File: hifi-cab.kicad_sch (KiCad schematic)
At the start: 0 parts

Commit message: Add RJ45
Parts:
- added J1: RJ45, symbol Connector:RJ45
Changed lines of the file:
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@@
 	(generator_version "9.0")
 	(paper "A4")
+	(symbol
+		(lib_id "Connector:RJ45")
+		(at 92.71 83.82 0)
+		(unit 1)
+		(exclude_from_sim no)
+		(in_bom yes)
+		(on_board yes)
+		(dnp no)
+		(fields_autoplaced yes)
+		(property "Reference" "J1"
+			(at 92.71 66.04 0)
+			(effects
+				(font
+					(size 1.27 1.27)
+				)
+			)
+		)
+		(property "Value" "RJ45"
+			(at 92.71 68.58 0)
+			(effects
+				(font
+					(size 1.27 1.27)
+				)
+			)
+		)
+		(property "Footprint" ""
+			(at 92.71 83.185 90)
+			(effects
+				(font
+					(size 1.27 1.27)
+				)
+				(hide yes)
+			)
+		)
+		(property "Datasheet" "~"
+			(at 92.71 83.185 90)
+			(effects
+				(font
+					(size 1.27 1.27)
+				)
+				(hide yes)
+			)
+		)
+		(property "Description" "RJ connector, 8P8C (8 positions 8 connected)"
+			(at 92.71 83.82 0)
+			(effects
+				(font
+					(size 1.27 1.27)
+				)
+				(hide yes)
+			)
+		)
+		(pin "2"
+		)
+		(pin "3"
+		)
+		(pin "1"
+		)
+		(pin "4"
+		)
+		(pin "5"
+		)
+		(pin "6"
+		)
+		(pin "7"
+		)
+		(pin "8"
+		)
+		(instances
+			(project ""
+				(path "/464ef4ad-8e38-4b55-beb7-b05b4d6675da"
+					(reference "J1")
+					(unit 1)
+				)
+			)
+		)
+	)
 	(sheet_instances
 		(path "/"

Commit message: Update hifi-cab.kicad_sch
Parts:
- removed J1: RJ45, symbol Connector:RJ45
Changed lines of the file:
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@@
 	(generator_version "9.0")
 	(paper "A4")
-	(symbol
-		(lib_id "Connector:RJ45")
-		(at 92.71 83.82 0)
-		(unit 1)
-		(exclude_from_sim no)
-		(in_bom yes)
-		(on_board yes)
-		(dnp no)
-		(fields_autoplaced yes)
-		(property "Reference" "J1"
-			(at 92.71 66.04 0)
-			(effects
-				(font
-					(size 1.27 1.27)
-				)
-			)
-		)
-		(property "Value" "RJ45"
-			(at 92.71 68.58 0)
-			(effects
-				(font
-					(size 1.27 1.27)
-				)
-			)
-		)
-		(property "Footprint" ""
-			(at 92.71 83.185 90)
-			(effects
-				(font
-					(size 1.27 1.27)
-				)
-				(hide yes)
-			)
-		)
-		(property "Datasheet" "~"
-			(at 92.71 83.185 90)
-			(effects
-				(font
-					(size 1.27 1.27)
-				)
-				(hide yes)
-			)
-		)
-		(property "Description" "RJ connector, 8P8C (8 positions 8 connected)"
-			(at 92.71 83.82 0)
-			(effects
-				(font
-					(size 1.27 1.27)
-				)
-				(hide yes)
-			)
-		)
-		(pin "2"
-		)
-		(pin "3"
-		)
-		(pin "1"
-		)
-		(pin "4"
-		)
-		(pin "5"
-		)
-		(pin "6"
-		)
-		(pin "7"
-		)
-		(pin "8"
-		)
-		(instances
-			(project ""
-				(path "/464ef4ad-8e38-4b55-beb7-b05b4d6675da"
-					(reference "J1")
-					(unit 1)
-				)
-			)
-		)
-	)
 	(sheet_instances
 		(path "/"

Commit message: V1 schematic
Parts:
- added D1, D2, D3, D4: 1N4004, Diode_THT:D_DO-41_SOD81_P10.16mm_Horizontal, symbol Diode:1N4004
- added J1: FAN 1, symbol Connector:USB_A
- added J10: BUTTON, symbol Connector:Conn_01x02_Pin
- added J11: RS-232, symbol Connector:Conn_01x04_Pin
- added J12: POWER IN, symbol Connector:Screw_Terminal_01x03
- added J2, J5: FAN VOLTAGE, symbol Connector:Conn_01x03_Pin
- added J3: FAN 1, symbol Connector:Screw_Terminal_01x04
- added J4: FAN 2, symbol Connector:USB_A
- added J6: FAN 2, symbol Connector:Screw_Terminal_01x04
- added J7: IR REMOTE, symbol Connector:Screw_Terminal_01x04
- added J8, J9: DS18B20, Connector_JST:JST_XH_B3B-XH-A_1x03_P2.50mm_Vertical, symbol Connector:Conn_01x03_Pin
- added Q1, Q2, Q3: AO3400A, Package_TO_SOT_SMD:SOT-23, symbol Transistor_FET:AO3400A
- added R1, R4, R7: 100R, Resistor_SMD:R_0805_2012Metric_Pad1.20x1.40mm_HandSolder, symbol Device:R
- added R10, R2, R5, R8: 10K, Resistor_SMD:R_0805_2012Metric_Pad1.20x1.40mm_HandSolder, symbol Device:R
- added R3, R6: 680R, symbol Device:R
- added R8: 68R, symbol Device:R
- added R9: 4K7, Resistor_THT:R_Axial_DIN0204_L3.6mm_D1.6mm_P7.62mm_Horizontal, symbol Device:R
- added U1: esp32-wemos-d1-mini, esp32-wemos-d1-mini:esp32-wemos-d1-mini, symbol esp32-wemos-d1-mini:esp32-wemos-d1-mini
- added U2: TSR1-2433E, Converter_DCDC:Converter_DCDC_TRACO_TSR1-xxxxE_THT, symbol Converter_DCDC:TSR1-2433E
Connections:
- new net: Q2.1 (G), R7.2
- new net: J7.1 (Pin_1), R8.1
- new net: Q1.1 (G), R1.2
- new net: J7.2 (Pin_2), J7.3 (Pin_3)
- new net: D2.2 (A), J2.2 (Pin_2), J3.2 (Pin_2)
- new net: Q3.1 (G), R4.2
- new net: D4.2 (A), J5.2 (Pin_2), J6.2 (Pin_2)
- new net +12V: J12.1 (Pin_1), J2.3 (Pin_3), J5.3 (Pin_3), U2.1 (Vin)
- new net +3.3V: J10.1 (Pin_1), J11.4 (Pin_4), J7.4 (Pin_4), J8.1 (Pin_1), J9.1 (Pin_1), R3.2, R6.2, R9.2, U1.16 (3V3), U2.3 (Vout)
- new net +5V: D1.2 (A), D3.2 (A), J1.1 (VBUS), J12.2 (Pin_2), J2.1 (Pin_1), J4.1 (VBUS), J5.1 (Pin_1), U1.35 (VCC_(USB))
- new net BTN_1: J10.2 (Pin_2), R10.1
- new net DS18B20: J8.2 (Pin_2), J9.2 (Pin_2), R9.1
- new net FAN1: D1.1 (K), D2.1 (K), J1.4 (GND), J1.5 (Shield), J3.1 (Pin_1), Q1.3 (D)
- new net FAN1_C: R1.1, R2.1
- new net FAN2: D3.1 (K), D4.1 (K), J4.4 (GND), J4.5 (Shield), J6.1 (Pin_1), Q3.3 (D)
- new net FAN2_C: R4.1, R5.1
- new net GND: J11.1 (Pin_1), J12.3 (Pin_3), J8.3 (Pin_3), J9.3 (Pin_3), Q1.2 (S), Q2.2 (S), Q3.2 (S), R10.2, R2.2, R5.2, R8.2, U1.1 (GND), U1.22 (GND), U1.33 (GND), U2.2 (GND)
- new net IR_1: Q2.3 (D), R8.2
- new net IR_C: R7.1, R8.1
- new net RPM1: J3.4 (Pin_4)
- new net RPM2: J6.4 (Pin_4)
- new net RX: J11.3 (Pin_3)
- new net TACH1: J3.3 (Pin_3), R3.1
- new net TACH2: J6.3 (Pin_3), R6.1
- new net TX: J11.2 (Pin_2)
- no-connect marks 0 -> 4
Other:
- note added: "5V BUS AT 0V IF POWERED >5V. MODULES MUST USE 3.3V."

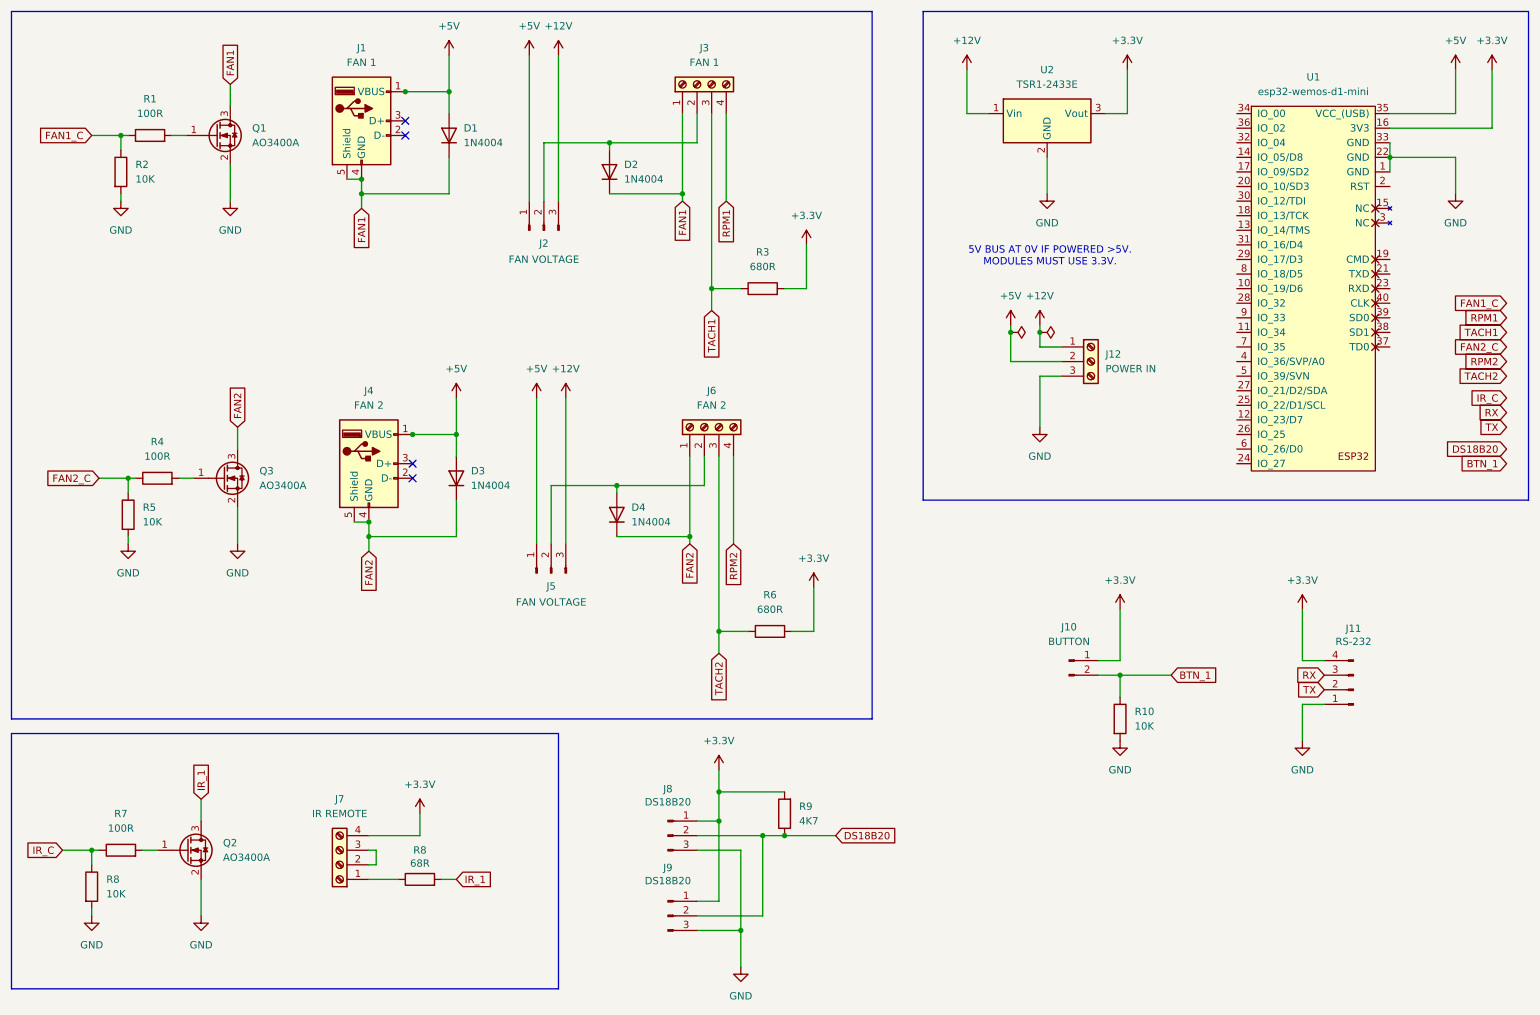
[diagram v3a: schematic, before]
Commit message: Switch some low current connectors to JSTs.
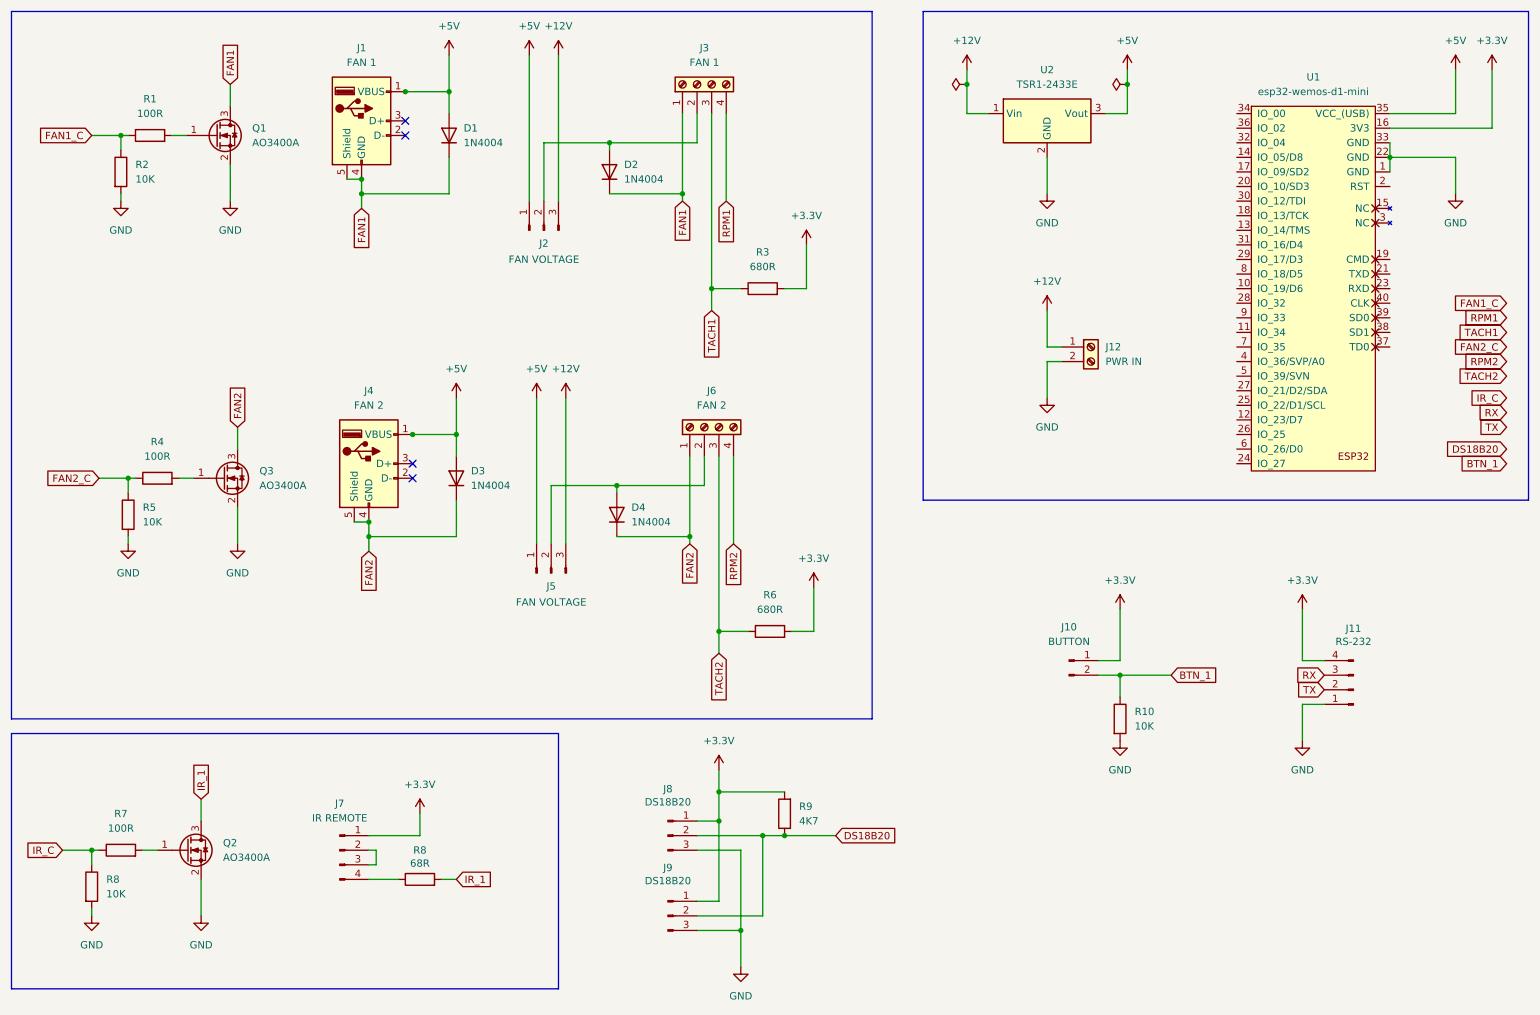
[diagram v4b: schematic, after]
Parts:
- removed J12: POWER IN, symbol Connector:Screw_Terminal_01x03
- added J12: PWR IN, symbol Connector:Screw_Terminal_01x02
- J7: symbol Connector:Screw_Terminal_01x04 -> Connector:Conn_01x04_Pin
- U2: symbol Converter_DCDC:TSR1-2433E -> Converter_DCDC:TSR1-2450E
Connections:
- net +12V: now also J12.1 (Pin_1)
- net +3.3V: now also J7.1 (Pin_1); no longer J7.4 (Pin_4), U2.3 (Vout)
- net +5V: now also U2.3 (Vout)
- net GND: now also J12.2 (Pin_2)
- net at R8.1: now also J7.4 (Pin_4); no longer J7.1 (Pin_1)
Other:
- note removed: "5V BUS AT 0V IF POWERED >5V. MODULES MUST USE 3.3V."

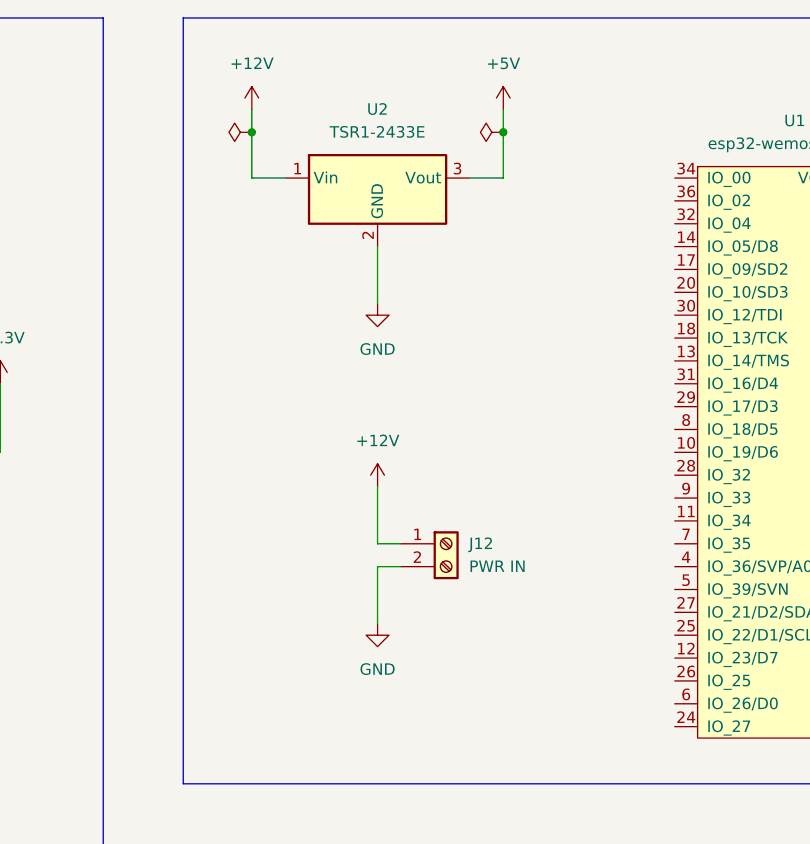
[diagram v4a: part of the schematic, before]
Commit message: Jumper on input voltage.
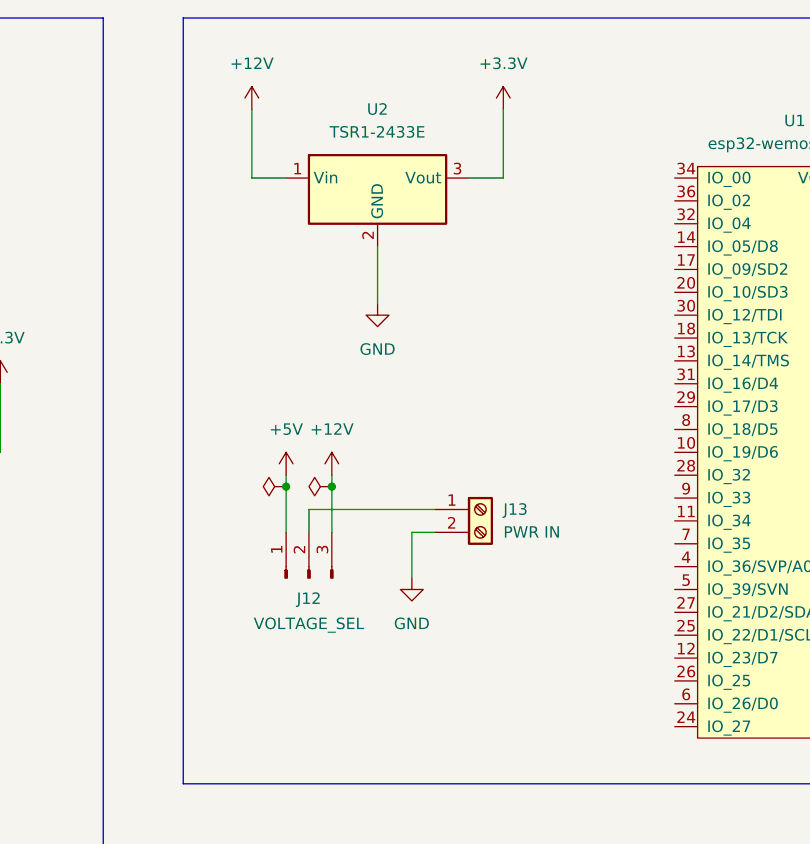
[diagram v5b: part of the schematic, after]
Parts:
- added J12: VOLTAGE_SEL, symbol Connector:Conn_01x03_Pin
- U2: symbol Converter_DCDC:TSR1-2450E -> Converter_DCDC:TSR1-2433E
- renumbered J12 to J13
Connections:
- net +12V: now also J12.3 (Pin_3); no longer J13.1 (Pin_1)
- net +3.3V: now also U2.3 (Vout)
- net +5V: now also J12.1 (Pin_1); no longer U2.3 (Vout)
- new net: J12.2 (Pin_2), J13.1 (Pin_1)
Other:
- moved on the sheet: J13

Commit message: Add note.
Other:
- note added: "5V BUS IS 0V WHERE 12V IS USED. MODULES MUST USE 3.3V."
- moved on the sheet: J12, J13, U2

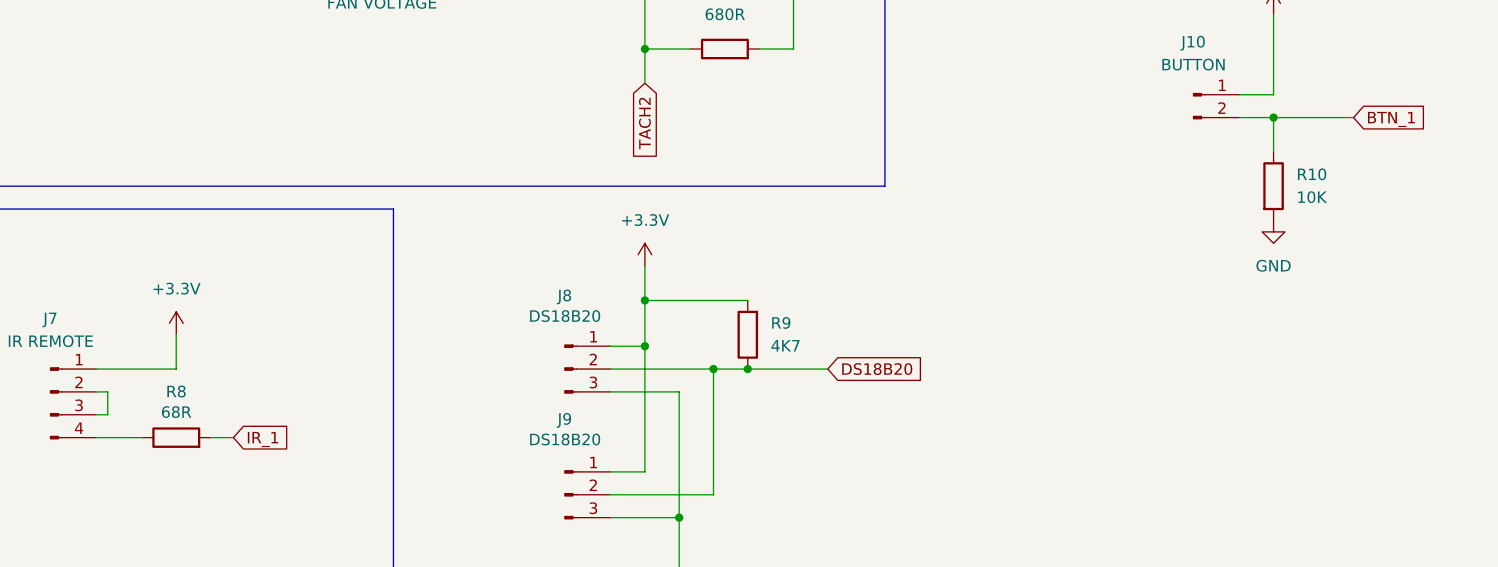
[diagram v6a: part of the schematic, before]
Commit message: Start assigning footprints.
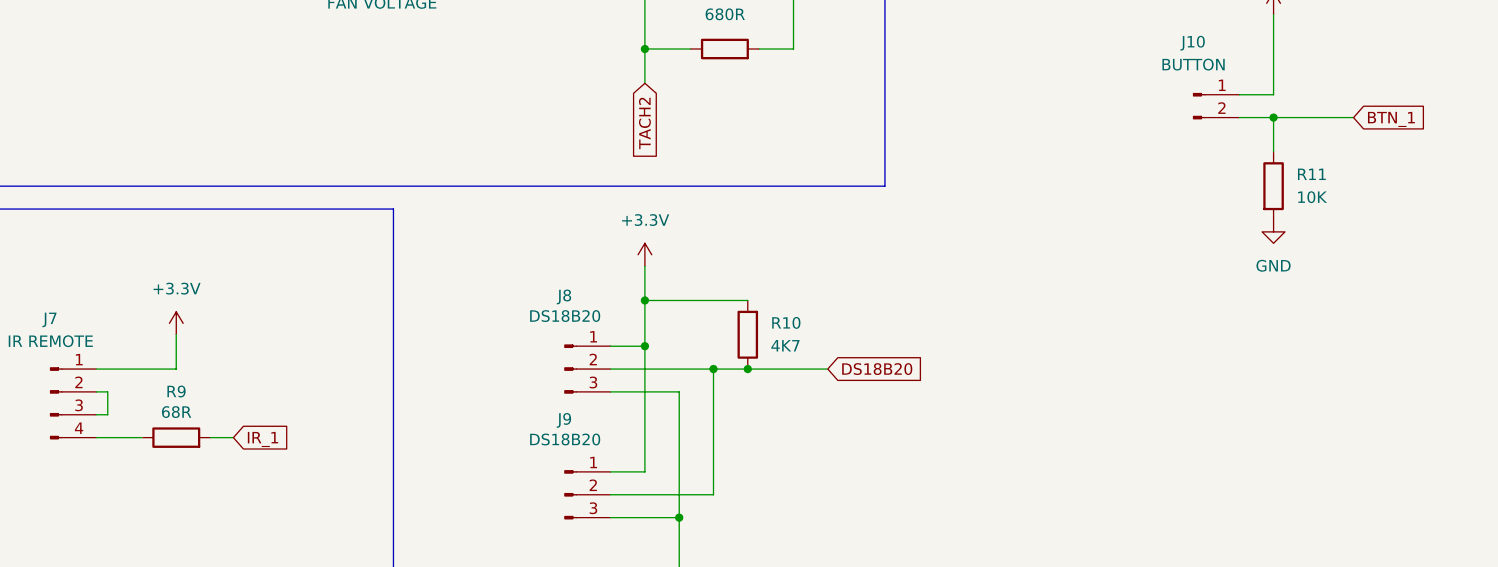
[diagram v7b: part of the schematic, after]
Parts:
- R10: renamed from R9; footprint Resistor_THT:R_Axial_DIN0204_L3.6mm_D1.6mm_P7.62mm_Horizontal -> Resistor_SMD:R_0805_2012Metric_Pad1.20x1.40mm_HandSolder
- R3, R6: footprint (none) -> Resistor_SMD:R_0805_2012Metric_Pad1.20x1.40mm_HandSolder
- R9: renamed from R8; footprint (none) -> Resistor_SMD:R_0805_2012Metric_Pad1.20x1.40mm_HandSolder
- renumbered R10 to R11
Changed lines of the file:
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@@
 		(dnp no)
 		(fields_autoplaced yes)
-		(property "Reference" "R10"
+		(property "Reference" "R11"
 			(at 210.82 138.4299 0)
 			(effects
@@
 			(project "hifi-cab"
 				(path "/464ef4ad-8e38-4b55-beb7-b05b4d6675da"
-					(reference "R10")
+					(reference "R11")
 					(unit 1)
 				)
@@
 			)
 		)
-		(property "Footprint" ""
+		(property "Footprint" "Resistor_SMD:R_0805_2012Metric_Pad1.20x1.40mm_HandSolder"
 			(at 147.32 126.238 90)
 			(effects
@@
 		(on_board yes)
 		(dnp no)
-		(property "Reference" "R8"
+		(property "Reference" "R9"
 			(at 86.36 162.56 90)
 			(effects
@@
 			)
 		)
-		(property "Footprint" ""
+		(property "Footprint" "Resistor_SMD:R_0805_2012Metric_Pad1.20x1.40mm_HandSolder"
 			(at 86.36 169.418 90)
 			(effects
@@
 			(project "hifi-cab"
 				(path "/464ef4ad-8e38-4b55-beb7-b05b4d6675da"
-					(reference "R8")
+					(reference "R9")
 					(unit 1)
 				)
@@
 		(dnp no)
 		(fields_autoplaced yes)
-		(property "Reference" "R9"
+		(property "Reference" "R10"
 			(at 152.4 154.9399 0)
 			(effects
@@
 			)
 		)
-		(property "Footprint" "Resistor_THT:R_Axial_DIN0204_L3.6mm_D1.6mm_P7.62mm_Horizontal"
+		(property "Footprint" "Resistor_SMD:R_0805_2012Metric_Pad1.20x1.40mm_HandSolder"
 			(at 151.638 156.21 90)
 			(effects
@@
 			(project "hifi-cab"
 				(path "/464ef4ad-8e38-4b55-beb7-b05b4d6675da"
-					(reference "R9")
+					(reference "R10")
 					(unit 1)
 				)
@@
 			)
 		)
-		(property "Footprint" ""
+		(property "Footprint" "Resistor_SMD:R_0805_2012Metric_Pad1.20x1.40mm_HandSolder"
 			(at 146.05 66.548 90)
 			(effects

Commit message: Update schematic.
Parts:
- J1, J4: footprint (none) -> USB_A1VSB6:ONSHORE_USB-A1VSB6
- J10, J13: footprint (none) -> Connector_JST:JST_XH_B2B-XH-A_1x02_P2.50mm_Vertical
- J11, J7: footprint (none) -> Connector_JST:JST_XH_B4B-XH-A_1x04_P2.50mm_Vertical
- J12, J2, J5: footprint (none) -> Connector_PinHeader_2.54mm:PinHeader_1x02_P2.54mm_Vertical
- J3, J6: footprint (none) -> Connector:FanPinHeader_1x04_P2.54mm_Vertical
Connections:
- net BTN_1: now also U1.7 (IO_35)
- net DS18B20: now also U1.11 (IO_34)
- net FAN1_C: now also U1.29 (IO_17/D3)
- net FAN2_C: now also U1.8 (IO_18/D5)
- net IR_C: now also U1.31 (IO_16/D4)
- net RPM1: now also U1.27 (IO_21/D2/SDA)
- net RPM2: now also U1.12 (IO_23/D7), U1.25 (IO_22/D1/SCL)
- net RX: now also U1.21 (TXD)
- net TACH1: now also U1.26 (IO_25)
- net TACH2: now also U1.6 (IO_26/D0)
- net TX: now also U1.23 (RXD)
- net +12V renamed VCC
- no-connect marks 4 -> 25
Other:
- note added: "5V BUS IS 0V WHERE VCC POWER IS USED."
- note removed: "5V BUS IS 0V WHERE 12V IS USED. MODULES MUST USE 3.3V."
- moved on the sheet: J2
